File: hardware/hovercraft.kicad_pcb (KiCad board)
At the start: 2 copper layers, 46.1 x 61.2 mm, 40 parts, among them J1 USB_OTG, J10 CONN_01X02, J11 CONN_01X02, J12 CONN_01X02, J2 CONN_01X03, J3 CONN_01X03, J4 CONN_01X03, J5 CONN_01X03, J6 CONN_01X03, J7 CONN_01X03, J8 CONN_01X02, J9 CONN_01X02, SW1 RESET, SW2 BOOT, U1 HC-12, U2 ATMEGA32U2-AU, Y1 Crystal_GND24

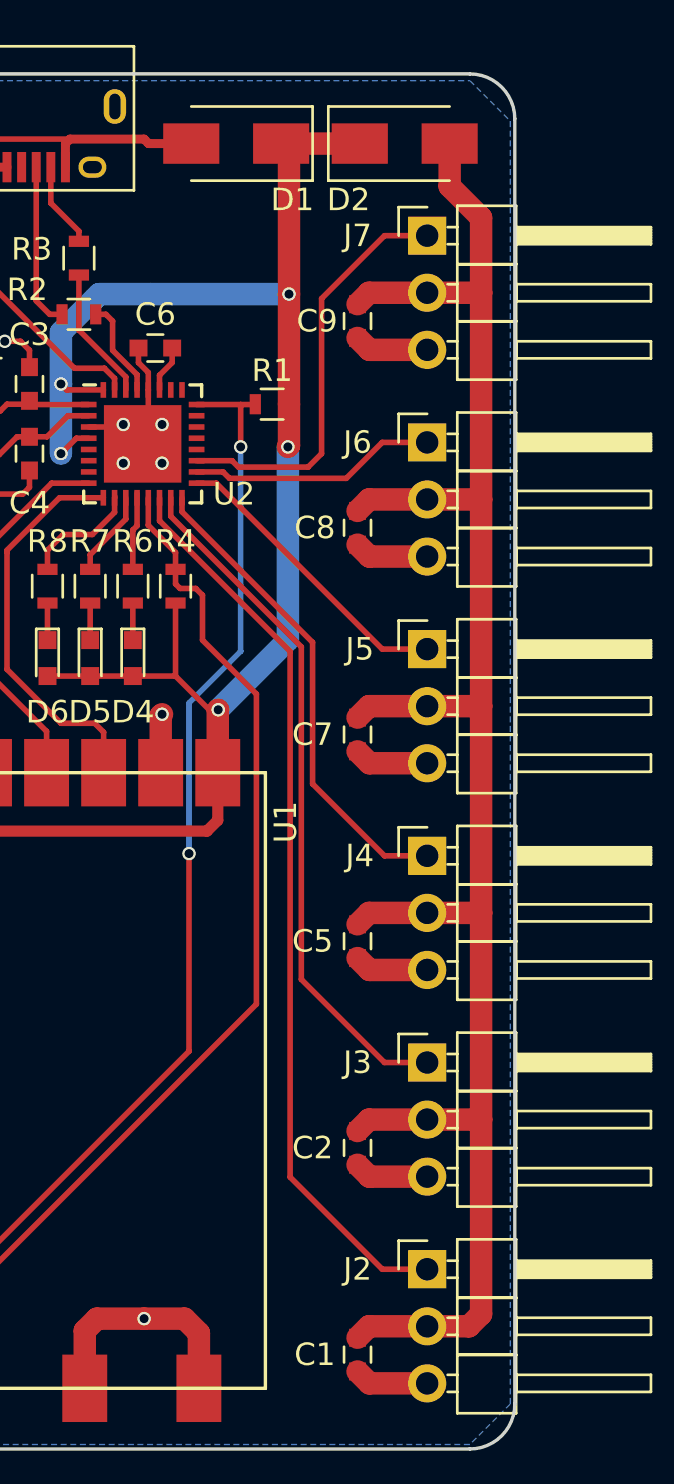
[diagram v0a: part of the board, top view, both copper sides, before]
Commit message: Increased some trace thicknesses around the servo connections to reduce thermal buildup
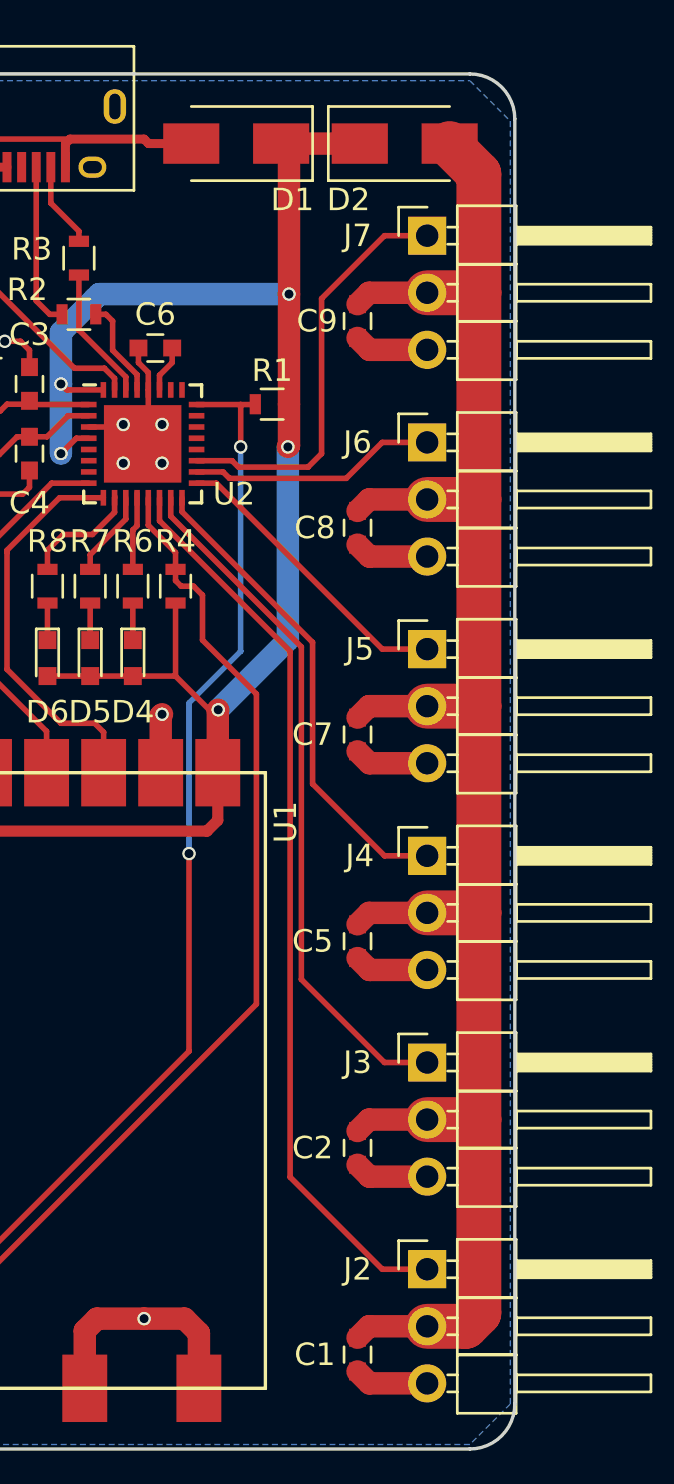
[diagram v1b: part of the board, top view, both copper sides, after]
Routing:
- net Net-(C1-Pad1): track 87.2 -> 86.5 mm
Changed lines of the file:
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@@
     (area 129.284999 65.854999 175.535001 127.205001)
     (thickness 1.6)
-    (drawings 13)
+    (drawings 12)
     (tracks 274)
     (zones 0)
@@
   )
   (setup
-    (last_trace_width 0.25)
+    (last_trace_width 2)
     (user_trace_width 0.4)
     (user_trace_width 0.5)
@@
     (pad_to_mask_clearance 0.2)
     (aux_axis_origin 0 0)
-    (grid_origin 140.76 150.23)
+    (grid_origin 193.96 100.88)
     (visible_elements 7FFFFF7F)
     (pcbplotparams
@@
     (arrow2a (pts (xy 185.926306 65.95037) (xy 185.338045 67.075914)))
     (arrow2b (pts (xy 185.926306 65.95037) (xy 186.510885 67.07783)))
-  )
-  (dimension 61.200082 (width 0.3) (layer Cmts.User)
-    (gr_text "61.200 mm" (at 190.86 96.53 270.0936205) (layer Cmts.User)
-      (effects (font (size 1.5 1.5) (thickness 0.3)))
-    )
-    (feature1 (pts (xy 131.46 127.13) (xy 121.277018 127.146639)))
-    (feature2 (pts (xy 131.36 65.93) (xy 121.177018 65.946639)))
-    (crossbar (pts (xy 123.877014 65.942227) (xy 123.977014 127.142227)))
-    (arrow1a (pts (xy 123.977014 127.142227) (xy 123.388753 126.016683)))
-    (arrow1b (pts (xy 123.977014 127.142227) (xy 124.561593 126.014767)))
-    (arrow2a (pts (xy 123.877014 65.942227) (xy 123.292435 67.069687)))
-    (arrow2b (pts (xy 123.877014 65.942227) (xy 124.465275 67.067771)))
   )
   (dimension 46.1 (width 0.3) (layer Cmts.User)
@@
   (segment (start 163.26 80.6451) (end 163.8949 80.6451) (width 0.25) (layer F.Cu) (net 20))
   (segment (start 163.8949 80.6451) (end 163.91 80.63) (width 0.25) (layer F.Cu) (net 20))
+  (segment (start 171.56 75.67) (end 173.86 75.67) (width 2) (layer F.Cu) (net 21) (status 400000))
+  (segment (start 171.56 84.87) (end 173.86 84.87) (width 2) (layer F.Cu) (net 21))
+  (segment (start 171.56 94.07) (end 173.86 94.07) (width 2) (layer F.Cu) (net 21))
+  (segment (start 171.56 103.27) (end 173.86 103.27) (width 2) (layer F.Cu) (net 21))
+  (segment (start 171.56 112.47) (end 173.86 112.47) (width 2) (layer F.Cu) (net 21))
+  (segment (start 172.56 69.03) (end 172.56 69.08) (width 2) (layer F.Cu) (net 21))
+  (segment (start 172.56 69.08) (end 173.86 70.38) (width 2) (layer F.Cu) (net 21))
+  (segment (start 173.86 70.38) (end 173.86 75.67) (width 2) (layer F.Cu) (net 21))
+  (segment (start 173.86 75.67) (end 173.86 84.87) (width 2) (layer F.Cu) (net 21))
+  (segment (start 173.86 84.87) (end 173.86 94.07) (width 2) (layer F.Cu) (net 21))
+  (segment (start 173.86 94.07) (end 173.86 103.27) (width 2) (layer F.Cu) (net 21))
+  (segment (start 173.86 103.27) (end 173.86 112.47) (width 2) (layer F.Cu) (net 21))
+  (segment (start 173.86 112.47) (end 173.86 121.08) (width 2) (layer F.Cu) (net 21))
+  (segment (start 173.27 121.67) (end 171.56 121.67) (width 2) (layer F.Cu) (net 21))
+  (segment (start 173.86 121.08) (end 173.27 121.67) (width 2) (layer F.Cu) (net 21))
   (segment (start 171.56 84.87) (end 168.97 84.87) (width 1) (layer F.Cu) (net 21))
   (segment (start 168.97 84.87) (end 168.46 85.38) (width 1) (layer F.Cu) (net 21))
@@
   (segment (start 171.56 103.27) (end 168.97 103.27) (width 1) (layer F.Cu) (net 21))
   (segment (start 168.97 103.27) (end 168.46 103.78) (width 1) (layer F.Cu) (net 21))
-  (segment (start 171.56 112.47) (end 173.96 112.47) (width 1) (layer F.Cu) (net 21))
-  (segment (start 171.56 103.27) (end 173.96 103.27) (width 1) (layer F.Cu) (net 21))
-  (segment (start 171.56 94.07) (end 173.96 94.07) (width 1) (layer F.Cu) (net 21))
-  (segment (start 171.56 84.87) (end 173.96 84.87) (width 1) (layer F.Cu) (net 21))
-  (segment (start 171.56 75.67) (end 173.96 75.67) (width 1) (layer F.Cu) (net 21))
-  (segment (start 171.56 121.67) (end 173.42 121.67) (width 1) (layer F.Cu) (net 21))
-  (segment (start 172.56 70.93) (end 172.56 69.03) (width 1) (layer F.Cu) (net 21))
-  (segment (start 173.96 72.33) (end 172.56 70.93) (width 1) (layer F.Cu) (net 21))
-  (segment (start 173.96 121.13) (end 173.96 112.47) (width 1) (layer F.Cu) (net 21))
-  (segment (start 173.96 112.47) (end 173.96 103.27) (width 1) (layer F.Cu) (net 21))
-  (segment (start 173.96 103.27) (end 173.96 94.07) (width 1) (layer F.Cu) (net 21))
-  (segment (start 173.96 94.07) (end 173.96 84.87) (width 1) (layer F.Cu) (net 21))
-  (segment (start 173.96 84.87) (end 173.96 75.67) (width 1) (layer F.Cu) (net 21))
-  (segment (start 173.96 75.67) (end 173.96 72.33) (width 1) (layer F.Cu) (net 21))
-  (segment (start 173.42 121.67) (end 173.96 121.13) (width 1) (layer F.Cu) (net 21))
   (segment (start 159.6473 79.9951) (end 159.6473 79.3427) (width 0.25) (layer F.Cu) (net 22))
   (segment (start 160.21 78.78) (end 160.21 78.13) (width 0.25) (layer F.Cu) (net 22))
@@
   (segment (start 163.96 93.53) (end 161.56 91.13) (width 0.25) (layer F.Cu) (net 28))
   (segment (start 161.56 91.13) (end 161.56 89.13) (width 0.25) (layer F.Cu) (net 28))
-  (segment (start 161.56 89.13) (end 161.26 88.83) (width 0.25) (layer F.Cu) (net 28))
-  (segment (start 161.26 88.83) (end 160.56 88.83) (width 0.25) (layer F.Cu) (net 28))
-  (segment (start 160.56 88.83) (end 160.36 88.63) (width 0.25) (layer F.Cu) (net 28))
-  (segment (start 160.36 88.63) (end 160.36 87.98) (width 0.25) (layer F.Cu) (net 28))
+  (segment (start 161.56 89.13) (end 161.16 88.73) (width 0.25) (layer F.Cu) (net 28))
+  (segment (start 161.16 88.73) (end 160.61 88.73) (width 0.25) (layer F.Cu) (net 28))
+  (segment (start 160.61 88.73) (end 160.36 88.48) (width 0.25) (layer F.Cu) (net 28))
+  (segment (start 160.36 88.48) (end 160.36 87.98) (width 0.25) (layer F.Cu) (net 28))
   (segment (start 147.485 123.805) (end 149.06 122.23) (width 0.25) (layer F.Cu) (net 28))
   (segment (start 147.485 124.48) (end 148.11 124.48) (width 0.25) (layer F.Cu) (net 28))
@@
   (segment (start 154.62 95.19) (end 152.16 92.73) (width 0.25) (layer F.Cu) (net 31))
   (zone (net 1) (net_name GND) (layer B.Cu) (hatch edge 0.508)
-    (connect_pads (clearance 0.3))
+    (connect_pads yes (clearance 0.3))
     (min_thickness 0.2)
-    (fill yes (arc_segments 16) (thermal_gap 0.3) (thermal_bridge_width 0.3))
+    (fill yes (arc_segments 16) (thermal_gap 0.3) (thermal_bridge_width 0.5))
     (polygon
       (pts

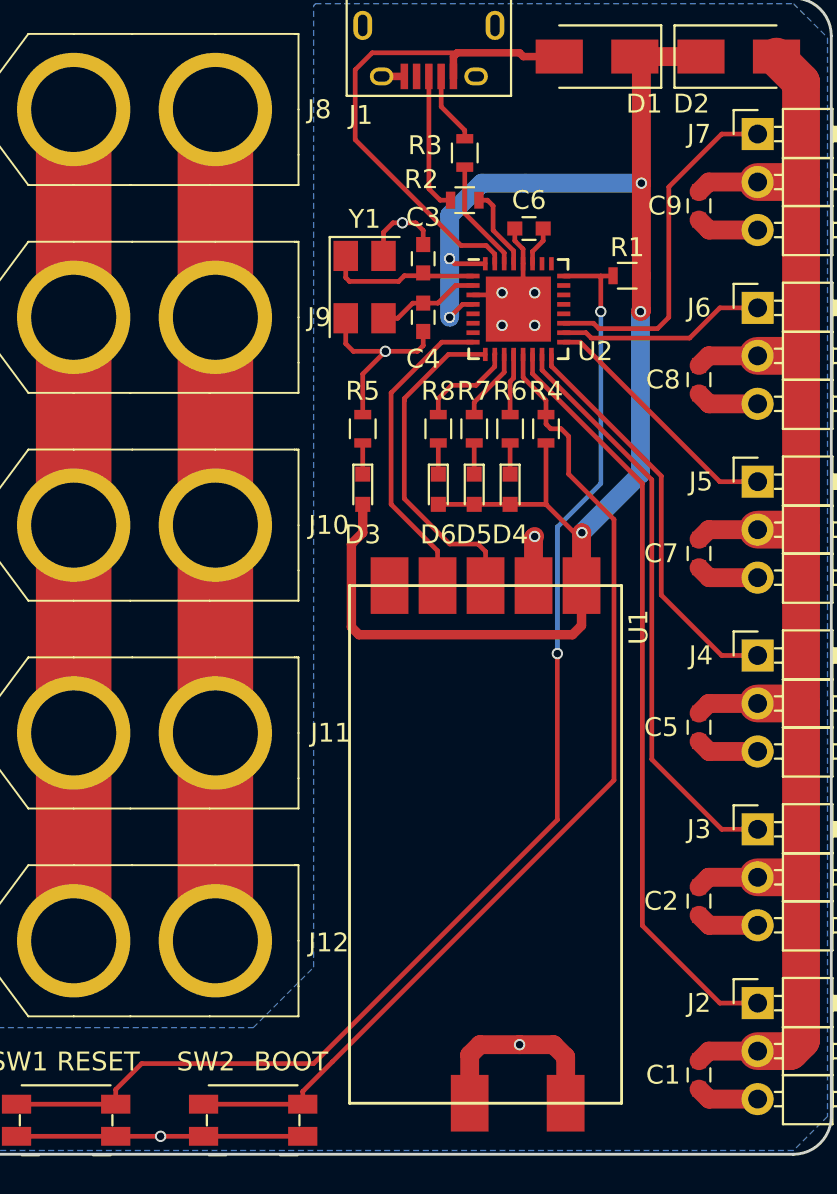
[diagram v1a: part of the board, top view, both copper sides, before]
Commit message: Separated some traces to try reduce crosstalk. Also added a name and version number to the board
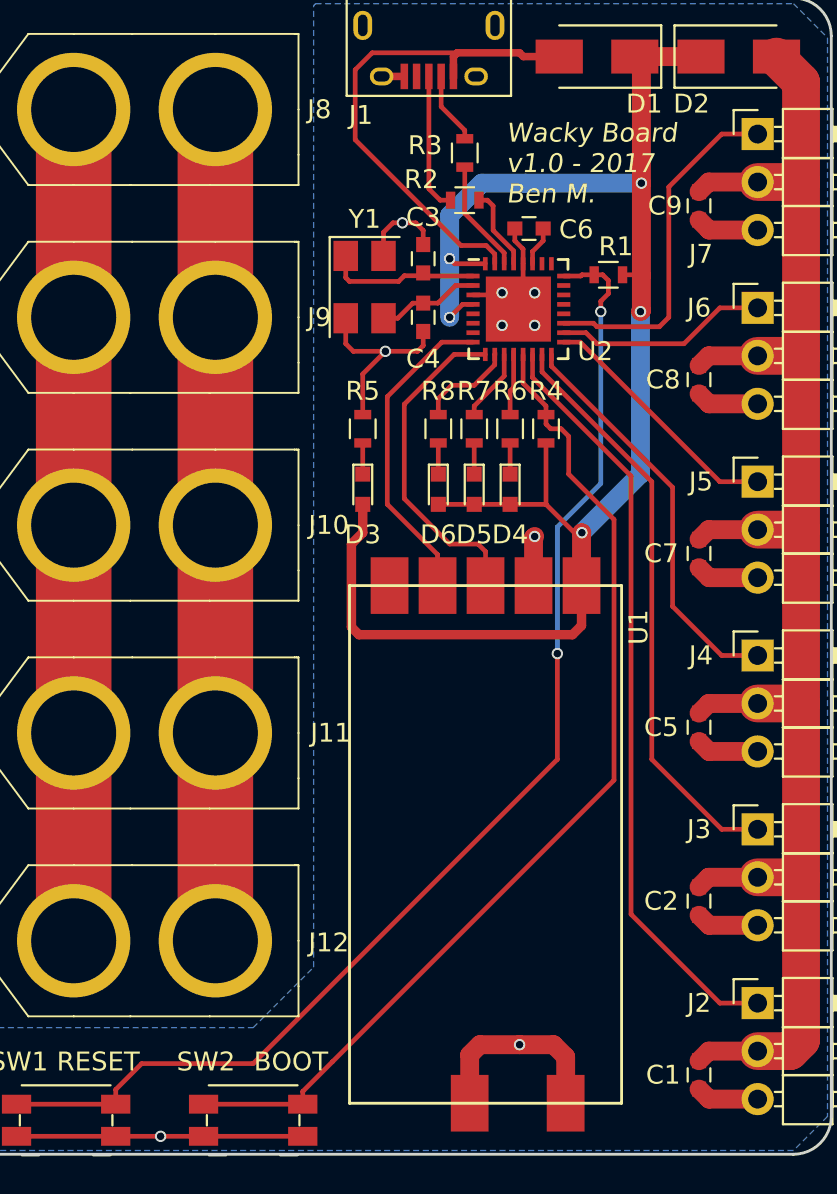
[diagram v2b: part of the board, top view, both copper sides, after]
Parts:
- moved R1 1.00 mm to (163.7, 80.6)
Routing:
- net Net-(R1-Pad2): track 67.7 -> 65.6 mm
- net VCC: track 85.6 -> 86.6 mm
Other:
- board text added: "Wacky Board v1.0 - 2017 Ben M."

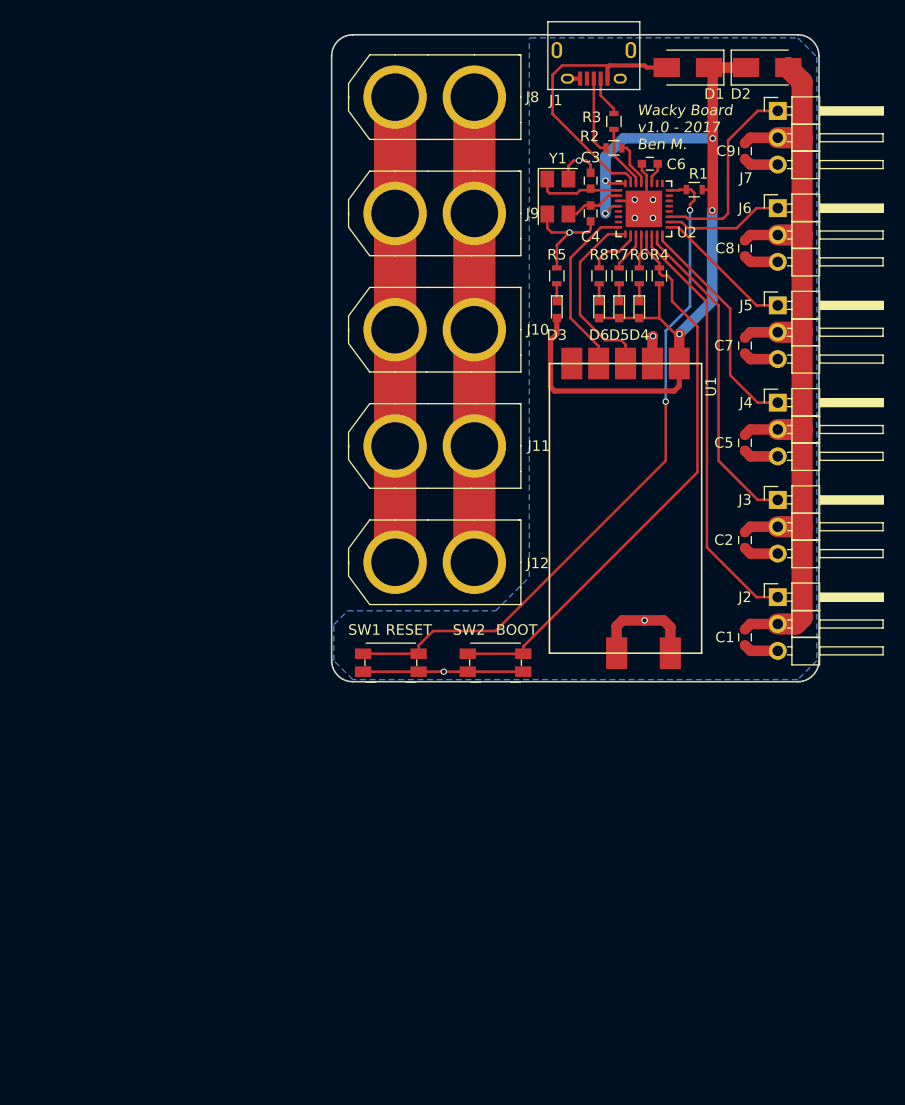
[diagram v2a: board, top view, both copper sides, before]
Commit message: Extend the board size to a more natural number and add mounting holes
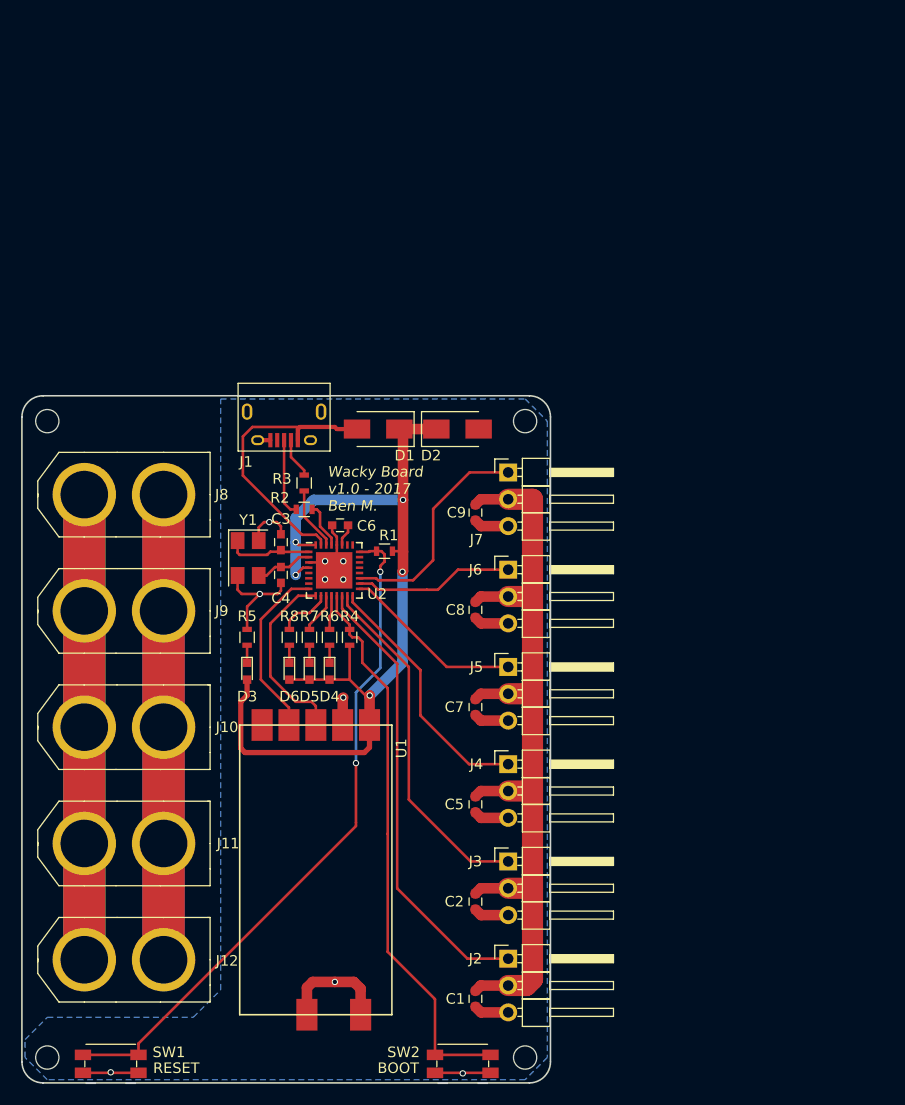
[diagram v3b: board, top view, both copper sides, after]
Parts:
- added REF**: MountingHole_2.2mm_M2, Mounting_Holes:MountingHole_2.2mm_M2, F.Cu at (102.5, 162.7)
- added REF**: MountingHole_2.2mm_M2, Mounting_Holes:MountingHole_2.2mm_M2, F.Cu at (147.7, 162.7)
- added REF**: MountingHole_2.2mm_M2, Mounting_Holes:MountingHole_2.2mm_M2, F.Cu at (147.7, 102.5)
- added REF**: MountingHole_2.2mm_M2, Mounting_Holes:MountingHole_2.2mm_M2, F.Cu at (102.5, 102.5)
- moved J10 47.7 mm to (106.0, 131.4)
- moved J11 47.7 mm to (106.0, 142.4)
- moved J12 47.7 mm to (106.0, 153.4)
- moved J8 47.7 mm to (106.0, 109.4)
- moved J9 47.7 mm to (106.0, 120.4)
- moved SW1 46.3 mm to (108.5, 163.3)
- moved C3 45.0 mm to (124.6, 113.9)
- moved C4 45.0 mm to (124.6, 117.0)
- moved C6 45.0 mm to (130.2, 112.3)
- moved D1 45.0 mm to (133.8, 103.2)
- moved D2 45.0 mm to (141.3, 103.2)
- moved R4 45.0 mm to (131.1, 122.9)
- moved R6 45.0 mm to (129.2, 122.9)
- moved U2 45.0 mm to (129.6, 116.6)
- moved D4 45.0 mm to (129.2, 126.1)
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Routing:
- net Net-(J10-Pad2): track 77.0 -> 121.0 mm
- net Net-(J10-Pad1): track 77.0 -> 121.0 mm
- net Net-(C1-Pad1): track 86.5 -> 79.3 mm
- net GND: track 69.8 -> 65.3 mm, vias 9 -> 10
- net /CH3: track 13.3 -> 17.1 mm
- net /CH4: track 11.3 -> 15.1 mm
- net /CH0: track 40.4 -> 43.1 mm
- net /CH2: track 21.6 -> 24.2 mm
- net /CH5: track 18.6 -> 21.2 mm
- net /CH1: track 31.0 -> 33.5 mm
- net Net-(R4-Pad1): track 54.7 -> 53.5 mm
- net Net-(R1-Pad2): track 65.6 -> 64.8 mm
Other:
- board size 46.1 x 61.2 mm -> 50 x 65 mm
